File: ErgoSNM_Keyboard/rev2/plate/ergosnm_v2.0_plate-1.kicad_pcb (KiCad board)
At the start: 2 copper layers, 116.3 x 111.5 mm, 5 parts

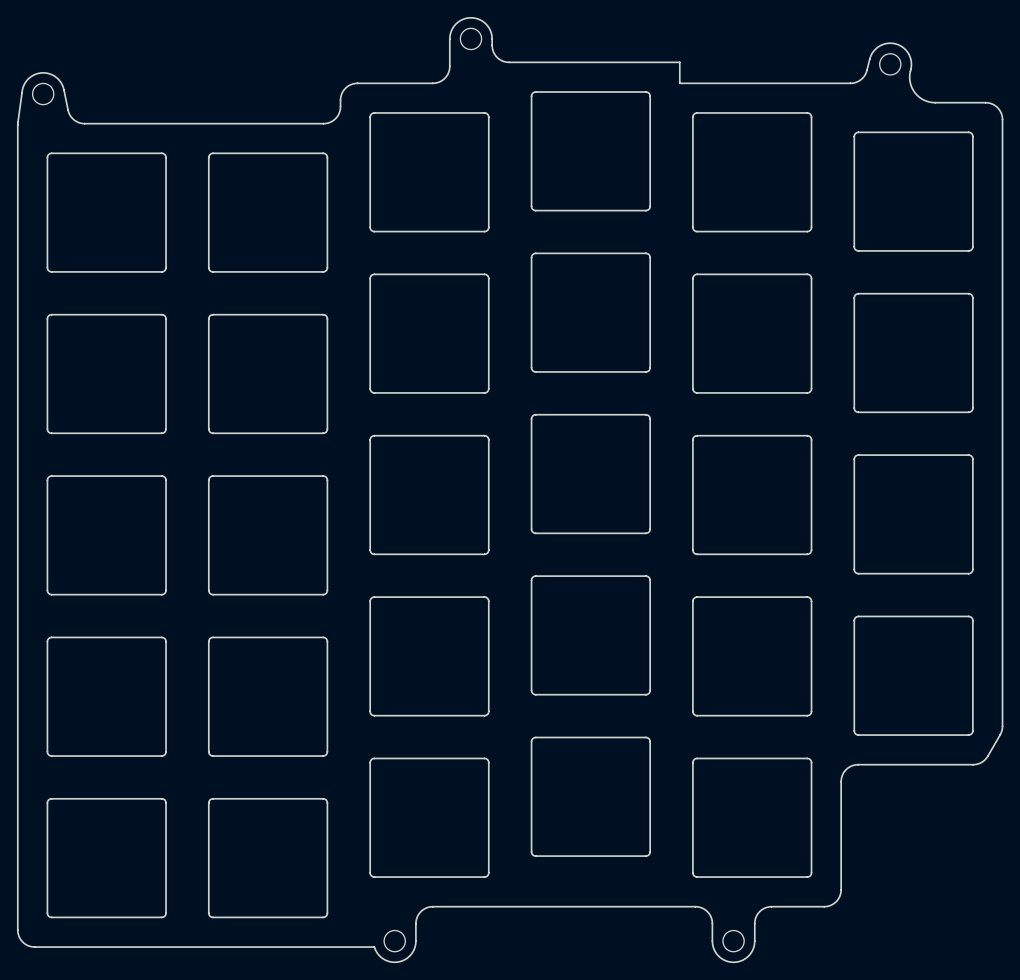
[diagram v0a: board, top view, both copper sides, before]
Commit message: Add mount holes to plate
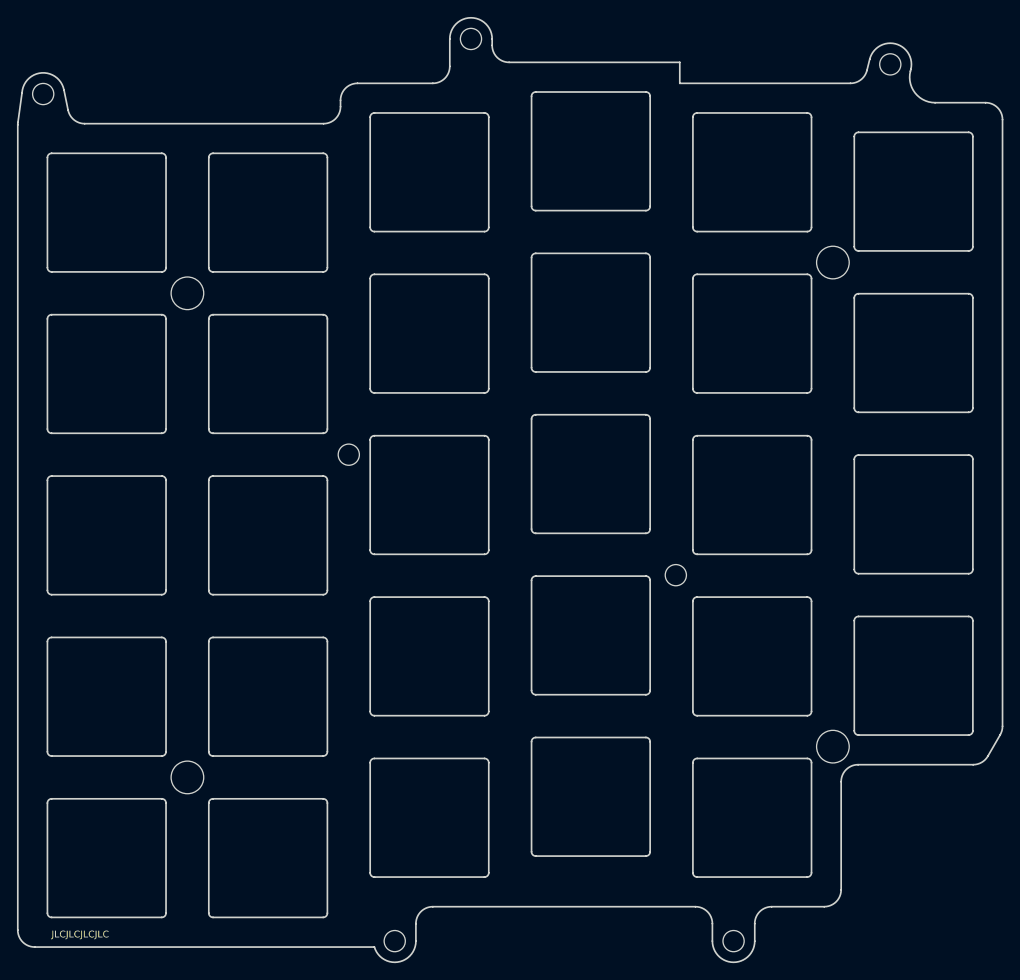
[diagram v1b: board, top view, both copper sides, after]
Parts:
- added REF**: MountingHole_3.7mm, MountingHole:MountingHole_3.7mm, F.Cu at (163.1, 68.0)
- added REF**: MountingHole_3.7mm, MountingHole:MountingHole_3.7mm, F.Cu at (86.9, 128.8)
- added REF**: MountingHole_2.5mm, MountingHole:MountingHole_2.5mm, F.Cu at (106.0, 90.7)
- added REF**: MountingHole_2.5mm, MountingHole:MountingHole_2.5mm, F.Cu at (144.6, 104.9)
- added REF**: MountingHole_3.7mm, MountingHole:MountingHole_3.7mm, F.Cu at (163.1, 125.2)
- added REF**: MountingHole_3.7mm, MountingHole:MountingHole_3.7mm, F.Cu at (86.9, 71.7)
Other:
- board text added: "JLCJLCJLCJLC"
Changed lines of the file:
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@@
   )
   (paper "A4")
+  (title_block
+    (title "ErgoSNM keyboard plate")
+    (rev "2.1")
+    (comment 1 "MIT License (open source hardware)")
+  )
   (layers
     (0 "F.Cu" signal)
@@
   )
   (net 0 "")
+  (footprint "MountingHole:MountingHole_3.7mm" (layer "F.Cu")
+    (at 163.1466 68.019)
+    (descr "Mounting Hole 3.7mm, no annular")
+    (tags "mounting hole 3.7mm no annular")
+    (attr exclude_from_pos_files exclude_from_bom)
+    (fp_text reference "REF**" (at 0 -4.7) (layer "F.SilkS") hide
+      (effects (font (size 1 1) (thickness 0.15)))
+    )
+    (fp_text value "MountingHole_3.7mm" (at 0 4.7) (layer "F.Fab")
+      (effects (font (size 1 1) (thickness 0.15)))
+    )
+    (fp_text user "${REFERENCE}" (at 0 0) (layer "F.Fab")
+      (effects (font (size 1 1) (thickness 0.15)))
+    )
+    (fp_circle (center 0 0) (end 3.7 0) (layer "Cmts.User") (width 0.15) (fill none))
+    (fp_circle (center 0 0) (end 3.95 0) (layer "F.CrtYd") (width 0.05) (fill none))
+    (pad "" np_thru_hole circle (at 0 0) (size 3.85 3.85) (drill 3.85) (layers F&B.Cu *.Mask))
+  )
+  (footprint "MountingHole:MountingHole_3.7mm" (layer "F.Cu")
+    (at 86.9466 128.801)
+    (descr "Mounting Hole 3.7mm, no annular")
+    (tags "mounting hole 3.7mm no annular")
+    (attr exclude_from_pos_files exclude_from_bom)
+    (fp_text reference "REF**" (at 0 -4.7) (layer "F.SilkS") hide
+      (effects (font (size 1 1) (thickness 0.15)))
+    )
+    (fp_text value "MountingHole_3.7mm" (at 0 4.7) (layer "F.Fab")
+      (effects (font (size 1 1) (thickness 0.15)))
+    )
+    (fp_text user "${REFERENCE}" (at 0 0) (layer "F.Fab")
+      (effects (font (size 1 1) (thickness 0.15)))
+    )
+    (fp_circle (center 0 0) (end 3.7 0) (layer "Cmts.User") (width 0.15) (fill none))
+    (fp_circle (center 0 0) (end 3.95 0) (layer "F.CrtYd") (width 0.05) (fill none))
+    (pad "" np_thru_hole circle (at 0 0) (size 3.85 3.85) (drill 3.85) (layers F&B.Cu *.Mask))
+  )
   (footprint "MountingHole:MountingHole_2.5mm" (layer "F.Cu")
     (at 69.9216 48.126)
@@
   )
   (footprint "MountingHole:MountingHole_2.5mm" (layer "F.Cu")
+    (at 105.9966 90.701)
+    (descr "Mounting Hole 2.5mm, no annular")
+    (tags "mounting hole 2.5mm no annular")
+    (attr exclude_from_pos_files exclude_from_bom)
+    (fp_text reference "REF**" (at 0 -3.5) (layer "F.SilkS") hide
+      (effects (font (size 1 1) (thickness 0.15)))
+    )
+    (fp_text value "MountingHole_2.5mm" (at 0 3.5) (layer "F.Fab")
+      (effects (font (size 1 1) (thickness 0.15)))
+    )
+    (fp_text user "${REFERENCE}" (at 0 0) (layer "F.Fab")
+      (effects (font (size 1 1) (thickness 0.15)))
+    )
+    (fp_circle (center 0 0) (end 2.5 0) (layer "Cmts.User") (width 0.15) (fill none))
+    (fp_circle (center 0 0) (end 2.75 0) (layer "F.CrtYd") (width 0.05) (fill none))
+    (pad "" np_thru_hole circle (at 0 0) (size 2.5 2.5) (drill 2.5) (layers *.Cu *.Mask))
+  )
+  (footprint "MountingHole:MountingHole_2.5mm" (layer "F.Cu")
+    (at 144.6046 104.925)
+    (descr "Mounting Hole 2.5mm, no annular")
+    (tags "mounting hole 2.5mm no annular")
+    (attr exclude_from_pos_files exclude_from_bom)
+    (fp_text reference "REF**" (at 0 -3.5) (layer "F.SilkS") hide
+      (effects (font (size 1 1) (thickness 0.15)))
+    )
+    (fp_text value "MountingHole_2.5mm" (at 0 3.5) (layer "F.Fab")
+      (effects (font (size 1 1) (thickness 0.15)))
+    )
+    (fp_text user "${REFERENCE}" (at 0 0) (layer "F.Fab")
+      (effects (font (size 1 1) (thickness 0.15)))
+    )
+    (fp_circle (center 0 0) (end 2.5 0) (layer "Cmts.User") (width 0.15) (fill none))
+    (fp_circle (center 0 0) (end 2.75 0) (layer "F.CrtYd") (width 0.05) (fill none))
+    (pad "" np_thru_hole circle (at 0 0) (size 2.5 2.5) (drill 2.5) (layers *.Cu *.Mask))
+  )
+  (footprint "MountingHole:MountingHole_3.7mm" (layer "F.Cu")
+    (at 163.1466 125.169)
+    (descr "Mounting Hole 3.7mm, no annular")
+    (tags "mounting hole 3.7mm no annular")
+    (attr exclude_from_pos_files exclude_from_bom)
+    (fp_text reference "REF**" (at 0 -4.7) (layer "F.SilkS") hide
+      (effects (font (size 1 1) (thickness 0.15)))
+    )
+    (fp_text value "MountingHole_3.7mm" (at 0 4.7) (layer "F.Fab")
+      (effects (font (size 1 1) (thickness 0.15)))
+    )
+    (fp_text user "${REFERENCE}" (at 0 0) (layer "F.Fab")
+      (effects (font (size 1 1) (thickness 0.15)))
+    )
+    (fp_circle (center 0 0) (end 3.7 0) (layer "Cmts.User") (width 0.15) (fill none))
+    (fp_circle (center 0 0) (end 3.95 0) (layer "F.CrtYd") (width 0.05) (fill none))
+    (pad "" np_thru_hole circle (at 0 0) (size 3.85 3.85) (drill 3.85) (layers F&B.Cu *.Mask))
+  )
+  (footprint "MountingHole:MountingHole_2.5mm" (layer "F.Cu")
     (at 120.4216 41.626)
     (descr "Mounting Hole 2.5mm, no annular")
@@
     (pad "" np_thru_hole circle (at 0 0) (size 2.5 2.5) (drill 2.5) (layers *.Cu *.Mask))
   )
+  (footprint "MountingHole:MountingHole_3.7mm" (layer "F.Cu")
+    (at 86.9466 71.651)
+    (descr "Mounting Hole 3.7mm, no annular")
+    (tags "mounting hole 3.7mm no annular")
+    (attr exclude_from_pos_files exclude_from_bom)
+    (fp_text reference "REF**" (at 0 -4.7) (layer "F.SilkS") hide
+      (effects (font (size 1 1) (thickness 0.15)))
+    )
+    (fp_text value "MountingHole_3.7mm" (at 0 4.7) (layer "F.Fab")
+      (effects (font (size 1 1) (thickness 0.15)))
+    )
+    (fp_text user "${REFERENCE}" (at 0 0) (layer "F.Fab")
+      (effects (font (size 1 1) (thickness 0.15)))
+    )
+    (fp_circle (center 0 0) (end 3.7 0) (layer "Cmts.User") (width 0.15) (fill none))
+    (fp_circle (center 0 0) (end 3.95 0) (layer "F.CrtYd") (width 0.05) (fill none))
+    (pad "" np_thru_hole circle (at 0 0) (size 3.85 3.85) (drill 3.85) (layers F&B.Cu *.Mask))
+  )
   (footprint "MountingHole:MountingHole_2.5mm" (layer "F.Cu")
     (at 151.4216 148.126)
@@
     (pad "" np_thru_hole circle (at 0 0) (size 2.5 2.5) (drill 2.5) (layers *.Cu *.Mask))
   )
+  (gr_circle locked (center 77.4216 62.126) (end 78.6916 64.031) (layer "Dwgs.User") (width 0.1) (fill none))
   (gr_line (start 145.0716 44.387) (end 145.0716 46.8635) (layer "Edge.Cuts") (width 0.2))
   (gr_arc (start 141.5716 80.437) (mid 141.425146 80.79053) (end 141.0716 80.937) (layer "Edge.Cuts") (width 0.2))
@@
   (gr_circle (center 111.4216 148.126) (end 112.6716 148.126) (layer "User.9") (width 0.2) (fill none))
   (gr_circle (center 151.4216 148.126) (end 152.6716 148.126) (layer "User.9") (width 0.2) (fill none))
+  (gr_text "JLCJLCJLCJLC" (at 74.295 147.32) (layer "F.SilkS")
+    (effects (font (size 0.8 0.8) (thickness 0.15)))
+  )
+  (group "" (id 23436daf-c0c4-4206-936f-6517c3e06ff0)
+    (members
+      12f6c021-b6f2-4297-b3ea-60185f37d8dd
+      20a8b42b-d600-4fa3-b907-729c85a25d45
+      42fb1ca6-802a-42a2-97d3-f3b5768e178e
+      6c794f0a-30b2-4192-98dc-556d373829a1
+      6f25c656-4481-42c0-8979-db198b159a8e
+      afd9ada7-cb84-4f88-bad5-9987166c2ae5
+      bc7f3e2f-5b28-428b-9773-6d1d071c216c
+      ddaa63dd-964c-495a-b65d-dcc522a46608
+    )
+  )
 )
